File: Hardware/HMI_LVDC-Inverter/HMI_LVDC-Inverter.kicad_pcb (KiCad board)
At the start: 2 copper layers, 83.6 x 76 mm, 130 parts, among them J1 Micro_PwrBus_B1, J10 Inv_Signal2_A1, J11 Conn_01x04_Pin, J2 Screw_Terminal_01x07, J3 START_BTN1, J4 TERMO_SW1, J5 STOP_BTN1, J6 SWD_Program1, J7 Inverter_MEAS, J8 Inv_Signal1_A1, J9 ESP32_Programmer, K1 RT174012, Q1 BC847, Q2 2N7002, SW1 SolderJumper_2_Open, U1 STM32F103C8Tx, U10 MCP23017_SO, U11 4N25, U12 4N25, U13 4N25, U14 4N25, U15 4N25, U16 4N25, U2 ESP32-WROOM-32E-N16, U3 AMS1117-3.3, U4 B1205S-2WR2, U5 AMS1117-3.3, U6 B1205S-2WR2, U7 4N25, U8 4N25, U9 PC817, Y1 Crystal 8MHz, Y2 32.768KHz

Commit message: Avance en el PCB
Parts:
- removed J2: Screw_Terminal_01x07, TerminalBlock_Phoenix:TerminalBlock_Phoenix_PT-1,5-7-5.0-H_1x07_P5.00mm_Horizontal
- added J4: Screw_Terminal_01x03, Footprints:MX250-3.5-03P-A-GY01-Cu-A, F.Cu at (81.0, 111.4)
- J3: value START_BTN1 -> Screw_Terminal_01x08; footprint TerminalBlock_Phoenix:TerminalBlock_Phoenix_MKDS-1,5-2_1x02_P5.00mm_Horizontal -> Footprints:MX250-3.5-08P-B-GY01-Cu-A
- J5: value STOP_BTN1 -> Conn_01x02; footprint TerminalBlock_Phoenix:TerminalBlock_Phoenix_MKDS-1,5-2_1x02_P5.00mm_Horizontal -> Connector_Molex:Molex_KK-254_AE-6410-02A_1x02_P2.54mm_Vertical
- moved J5 71.4 mm to (40.5, 100.0), turned to 0 degrees
- moved J3 30.2 mm to (93.0, 110.7), turned to 0 degrees
- moved C22 24.6 mm to (130.0, 50.1), turned to 180 degrees
- moved R21 19.6 mm to (130.0, 54.8), turned to 0 degrees
- moved R23 17.4 mm to (130.0, 57.3), turned to 0 degrees
- moved Q1 16.0 mm to (130.0, 59.3), turned to -90 degrees
- moved U7 14.5 mm to (129.9, 66.2), turned to -90 degrees
- moved Q2 12.5 mm to (125.3, 57.3), turned to 0 degrees
- moved R28 11.7 mm to (74.9, 75.3)
- moved U8 11.7 mm to (68.7, 72.8)
- moved R24 10.6 mm to (122.5, 57.3), turned to 90 degrees
- moved D4 10.0 mm to (69.2, 79.0)
- moved K1 10.0 mm to (68.8, 94.9)
- moved C21 9.97 mm to (125.0, 69.2), turned to 90 degrees
- moved R25 9.87 mm to (125.3, 59.9), turned to 0 degrees
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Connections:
- J3 pad 1: GND_ISO -> /Perifericos/FREQ_SEL_1_ISO
- J3 pad 2: /Perifericos/START_CTRL_ISO -> /Perifericos/FREQ_SEL_2_ISO
- J5 pad 1: GND_ISO -> /Perifericos/TERMO_SWITCH_ISO
- J5 pad 2: /Perifericos/STOP_BUTTON_ISO -> GND_ISO
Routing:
- net /Perifericos/RELAY_NC: track 22.8 -> 0.00 mm
- net +12V_ISO: track 134.6 -> 112.1 mm
- net GND_ISO: track 28.3 -> 8.27 mm
- net /Perifericos/RELAY_COM: track 18.2 -> 0.00 mm
- net /Perifericos/STOP_BUTTON_ISO: track 18.6 -> 2.05 mm
- net /Perifericos/FREQ_SEL_1_ISO: track 16.3 -> 2.16 mm
- net /Perifericos/START_CTRL_ISO: track 15.9 -> 2.23 mm
- net /Perifericos/FREQ_SEL_4_ISO: track 15.7 -> 2.24 mm
- net /Perifericos/RELAY_NO: track 13.6 -> 2.63 mm
- net /Perifericos/FREQ_SEL_3_ISO: track 13.1 -> 2.27 mm
- net /Perifericos/FREQ_SEL_2_ISO: track 13.8 -> 4.03 mm
- net Net-(D4-A): track 11.0 -> 7.62 mm

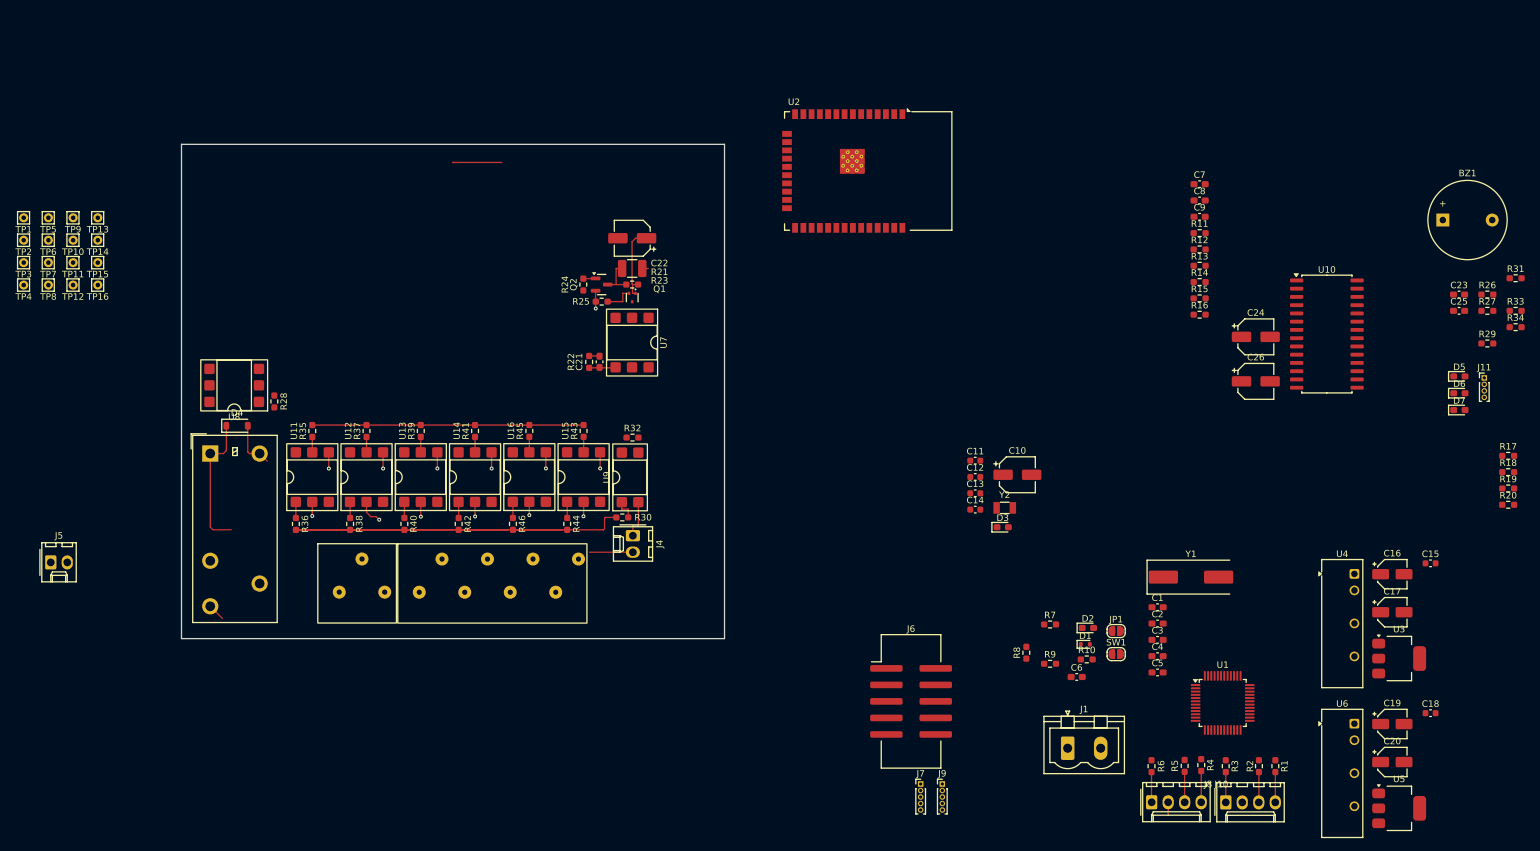
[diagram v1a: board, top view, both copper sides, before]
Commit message: Falta resolver los pulsadores
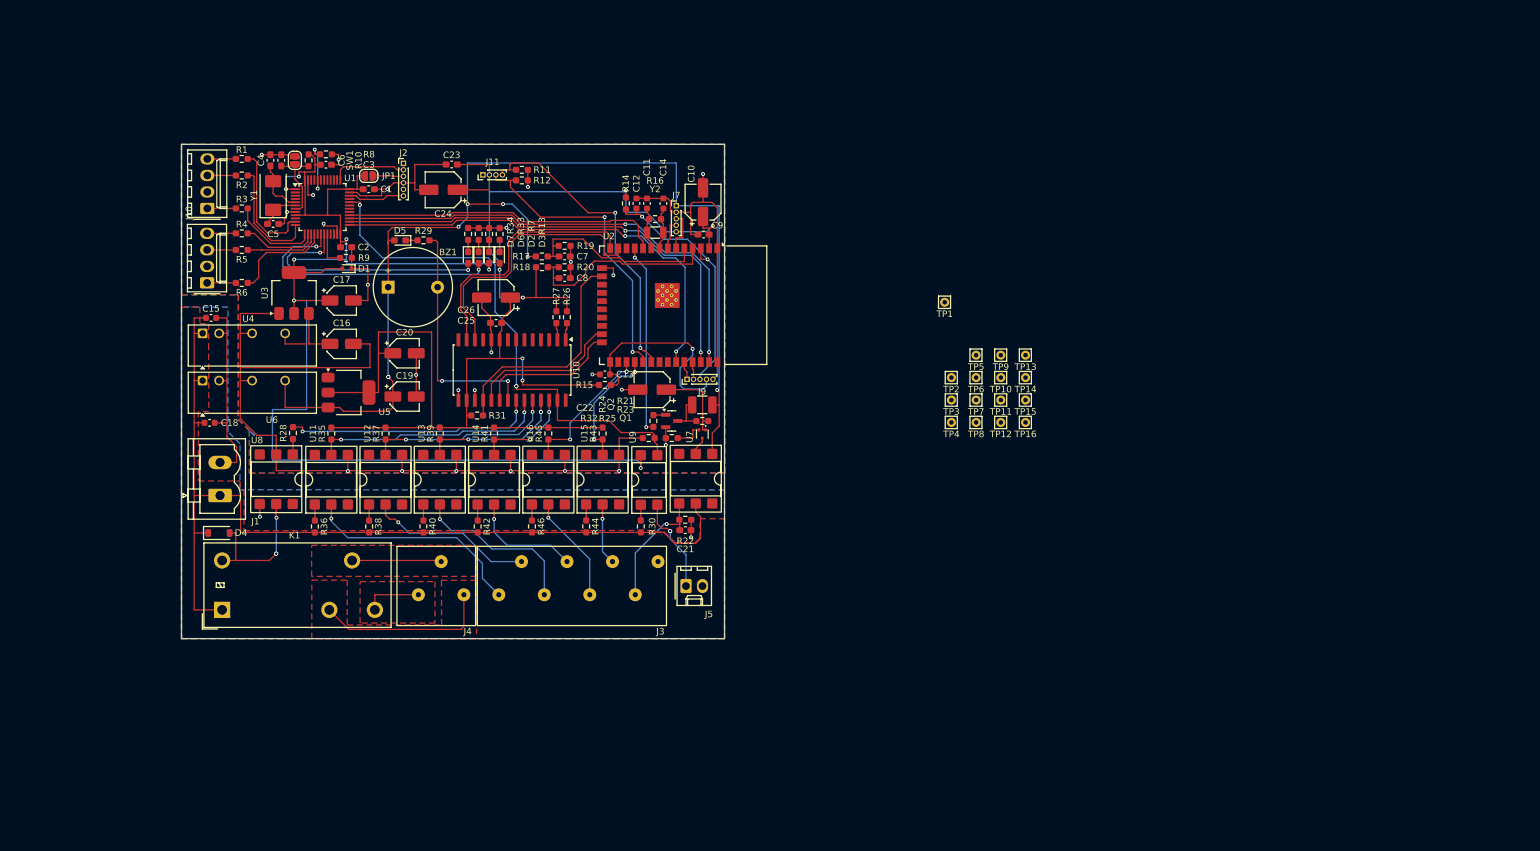
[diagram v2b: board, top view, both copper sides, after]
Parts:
- removed the J4 at (130.1, 95.9)
- removed J6: SWD_Program1, Connector_IDC:IDC-Header_2x05_P2.54mm_Vertical_SMD
- added J2: Conn_01x06_Pin, Connector_PinHeader_1.00mm:PinHeader_1x06_P1.00mm_Vertical, F.Cu at (94.8, 38.6)
- Y1: footprint Crystal:Crystal_SMD_HC49-SD -> Crystal:Crystal_SMD_0603-2Pin_6.0x3.5mm
- moved C18 193.1 mm to (65.0, 78.5)
- moved C15 191.4 mm to (65.2, 62.4)
- moved U6 184.9 mm to (63.9, 72.0), turned to 90 degrees
- moved R1 184.4 mm to (69.9, 38.0), turned to 180 degrees
- moved J8 181.4 mm to (64.6, 45.6), turned to 90 degrees
- moved U4 181.0 mm to (63.9, 64.8), turned to 90 degrees
- moved R2 181.0 mm to (69.9, 40.5), turned to 180 degrees
- moved U3 179.1 mm to (77.9, 58.6), turned to 90 degrees
- moved R3 174.0 mm to (69.9, 45.6), turned to 180 degrees
- moved U5 173.9 mm to (86.3, 73.9)
- moved R4 168.8 mm to (69.9, 49.4), turned to 180 degrees
- moved C17 168.6 mm to (85.3, 59.7)
- moved J10 165.9 mm to (64.6, 57.0), turned to 90 degrees
- moved C16 165.5 mm to (85.3, 66.4)
- moved R5 165.4 mm to (69.9, 52.0), turned to 180 degrees
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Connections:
- D3 pad 2: unconnected-(D3-A-Pad2) -> +3.3V_ESP
- J4 pad 1: /Perifericos/RELAY_COM -> /Perifericos/RELAY_NO
- J4 pad 2: /Perifericos/RELAY_NC -> /Perifericos/RELAY_COM
- J4 pad 3: /Perifericos/RELAY_NO -> /Perifericos/RELAY_NC
- R17 pad 1: unconnected-(R17-Pad1) -> +5V_ESP
- R18 pad 1: unconnected-(R18-Pad1) -> +3.3V_ESP
- U1 pad 37: /SW_Clik -> /STM32/SW_Clk
- U10 pad 24: /Perifericos/FREQ_SEL_1 -> /Perifericos/FREQ_SEL_2
- U2 pad 23: /ESP32/INT_A -> /ESP32/INT_B
- U2 pad 24: /ESP32/INT_B -> /ESP32/INT_A
- U9 pad 4: unconnected-(U9-Pad4) -> 3V3_STM
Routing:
- net GND: track 19.6 -> 290.6 mm, vias 7 -> 25
- net 3V3_STM: track 0.00 -> 193.3 mm, vias 0 -> 7
- net +3.3V_ESP: track 41.7 -> 232.4 mm, vias 0 -> 6
- net +5V_ESP: track 8.53 -> 175.2 mm, vias 0 -> 7
- net /Perifericos/TermoSw_Input: track 0.00 -> 80.1 mm, vias 0 -> 3
- net /ESP32/MISO: track 0.00 -> 73.2 mm, vias 0 -> 2
- net /ESP32/SCK: track 0.00 -> 72.2 mm, vias 0 -> 2
- net /ESP32/NSS: track 0.00 -> 70.0 mm, vias 0 -> 2
- net /ESP32/MOSI: track 0.00 -> 49.4 mm
- net /ESP32/OLED_SDA: track 0.00 -> 48.5 mm, vias 0 -> 2
- net /ESP32/OLED_SCL: track 0.00 -> 46.6 mm, vias 0 -> 2
- net /ESP32/SCL_MCP: track 0.00 -> 42.7 mm
- net /Perifericos/LED_State: track 0.00 -> 42.1 mm, vias 0 -> 2
- net /ESP32/SDA_MCP: track 0.00 -> 40.0 mm
- net /ESP32/ENABLE: track 0.00 -> 39.7 mm, vias 0 -> 2
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- added copper zone on F.Cu, net +12V_ISO
- added copper zone on F.Cu, net /Perifericos/RELAY_COM
- added copper zone on F.Cu, net /Perifericos/RELAY_NC
- added copper zone on F.Cu, net /Perifericos/RELAY_NO
- added copper zone on B.Cu, net GND
- added copper zone on F.Cu, net GND
- added copper zone on B.Cu, net GND_ISO

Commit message: Agregado y corrección de borneras
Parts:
- added SW2: SW_MEC_5G, Footprints:SW_Push_SPST_NO_Alps_SKRK, F.Cu at (200.1, 54.8)
- added SW3: SW_MEC_5G, Footprints:SW_Push_SPST_NO_Alps_SKRK, F.Cu at (200.1, 59.3)
- added SW4: SW_MEC_5G, Footprints:SW_Push_SPST_NO_Alps_SKRK, F.Cu at (200.1, 63.7)
- added SW5: SW_MEC_5G, Footprints:SW_Push_SPST_NO_Alps_SKRK, F.Cu at (200.1, 68.2)
- added SW6: SW_MEC_5G, Footprints:SW_Push_SPST_NO_Alps_SKRK, F.Cu at (200.1, 72.6)
- added SW7: SW_MEC_5G, Footprints:SW_Push_SPST_NO_Alps_SKRK, F.Cu at (200.1, 77.1)
- added SW8: SW_MEC_5G, Footprints:SW_Push_SPST_NO_Alps_SKRK, F.Cu at (200.1, 81.5)
- added SW9: SW_MEC_5G, Footprints:SW_Push_SPST_NO_Alps_SKRK, F.Cu at (200.1, 86.0)
- TP1, TP10, TP11, TP12, TP13, TP14, TP15, TP16, TP2, TP3, TP4, TP5, TP6, TP7, TP8, TP9: footprint Connector_Pin:Pin_D0.7mm_L6.5mm_W1.8mm_FlatFork -> TestPoint:TestPoint_Pad_D1.0mm
- Y1: footprint Crystal:Crystal_SMD_0603-2Pin_6.0x3.5mm -> Crystal:Crystal_SMD_5032-2Pin_5.0x3.2mm
- moved TP1 8.24 mm to (179.1, 68.2)
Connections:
- TP15 pad 1: unconnected-(TP15-Pad1) -> /ESP32/OLED_SDA
- TP16 pad 1: unconnected-(TP16-Pad1) -> /ESP32/OLED_SCL
